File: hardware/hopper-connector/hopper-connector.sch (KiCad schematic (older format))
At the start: 17 parts, among them P1 CONN_01X02, P2 CONN_01X02, P3 CONN_01X05, P4 CONN_01X04, P5 CONN_01X04, Q1 BTS430K2, Q2 BC807-40, U1 LTV-817, U2 LTV-817, U3 LTV-817

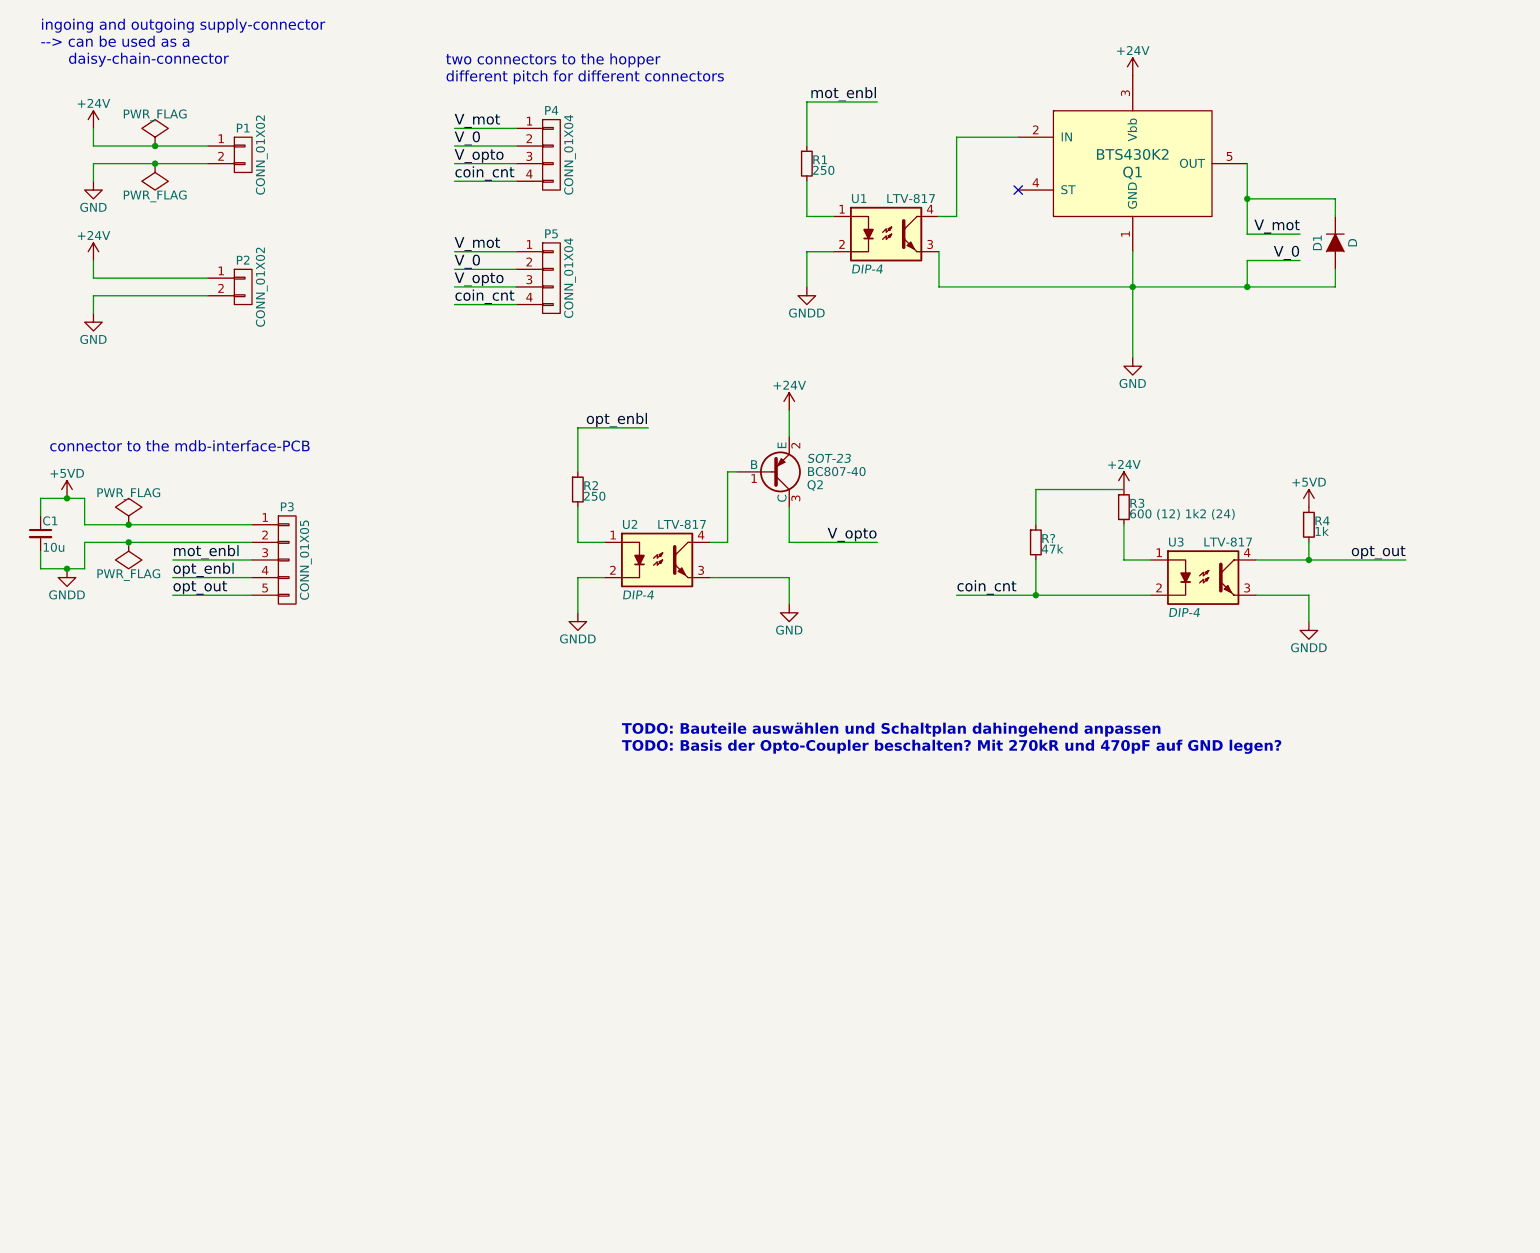
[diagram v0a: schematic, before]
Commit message: circuit now with better couplers and fuse
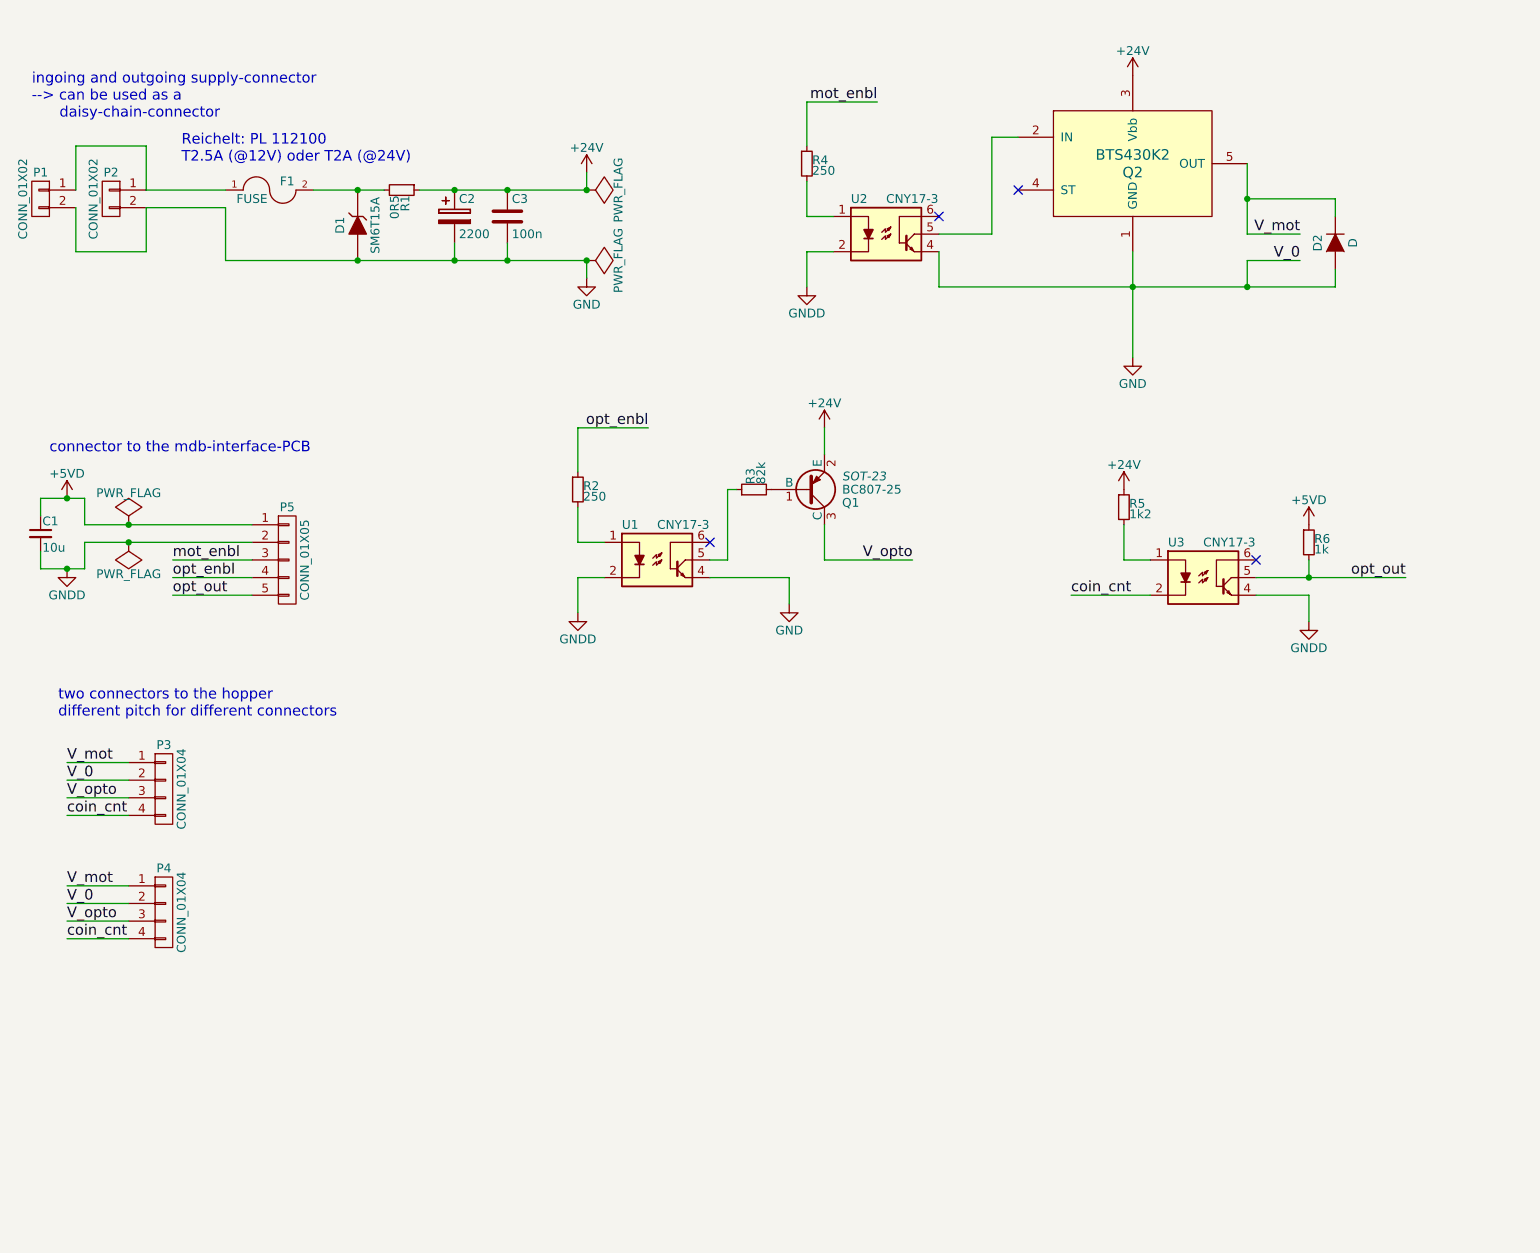
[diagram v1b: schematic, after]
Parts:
- removed R?: 47k, symbol R_Small
- removed U1, U2, U3: LTV-817, DIP-4, symbol LTV-817
- added C2: 2200, symbol CP
- added C3: 100n, symbol C
- added D1: SM6T15A, symbol ZENER
- added F1: FUSE, symbol FUSE
- added R1: 0R5, symbol R_Small
- added R3: 82k, symbol R_Small
- added U1, U2, U3: CNY17-3, symbol CNY17-3
- Q1: renamed from Q2; value BC807-40 -> BC807-25
- R5: renamed from R3; value 600 (12) 1k2 (24) -> 1k2
- renumbered D1 to D2, P2 to P1, P1 to P2, P4 to P3, P5 to P4, P3 to P5, Q1 to Q2, R1 to R4, R4 to R6
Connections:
- net +24V: now also C2.1, C3.1, R1.1; no longer P1.1 (P1), P2.1 (P1)
- net GND: now also C2.2, C3.2, D1.1 (A), U1.4, U2.4
- net GNDD: now also U1.2, U2.2, U3.4
- net coin_cnt: now also U3.2
- net opt_out: now also U3.5
- net at R4.2: now also U2.1
- net at Q2.2 (IN): now also U2.5
- net at R2.2: now also U1.1
- net at Q1.1 (B): now also R3.2
- net at R5.2: now also U3.1
- new net: F1.1, P1.1 (P1), P2.1 (P1)
- new net: R3.1, U1.5
- new net: D1.2 (K), F1.2, R1.2
- no-connect marks 1 -> 4
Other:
- note added: "Reichelt: PL 112100\nT2.5A (@12V) oder T2A (@24V)"
- note removed: "TODO: Bauteile auswählen und Schaltplan dahingehend anpassen\nTODO: Basis der Opto-Coupler beschalten? Mit 270kR und 470pF auf GND legen?"
- moved on the sheet: P1, P2, P3, P4, Q1, R6

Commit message: first real version of schematic
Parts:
- D2: value D -> 1N4004
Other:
- note added: "use stronger TRANSIL?\nThis one will burn before fuse triggers.\n(Only really relevant in case of wrong polarity\nof power supply) Datasheet says the diode\nfails short so at least the protection works..."
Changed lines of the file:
@@
 P 8050 1750
 F 0 "D2" H 8050 1850 50  0000 C CNN
-F 1 "D" H 8050 1650 50  0000 C CNN
+F 1 "1N4004" H 8050 1650 50  0000 C CNN
 F 2 "" H 8050 1750 60  0000 C CNN
 F 3 "" H 8050 1750 60  0000 C CNN
@@
 Connection ~ 3800 1450
 Connection ~ 3800 1850
+Text Notes 2200 2050 0    20   ~ 0
+use stronger TRANSIL?\nThis one will burn before fuse triggers.\n(Only really relevant in case of wrong polarity\nof power supply) Datasheet says the diode\nfails short so at least the protection works...
 $EndSCHEMATC

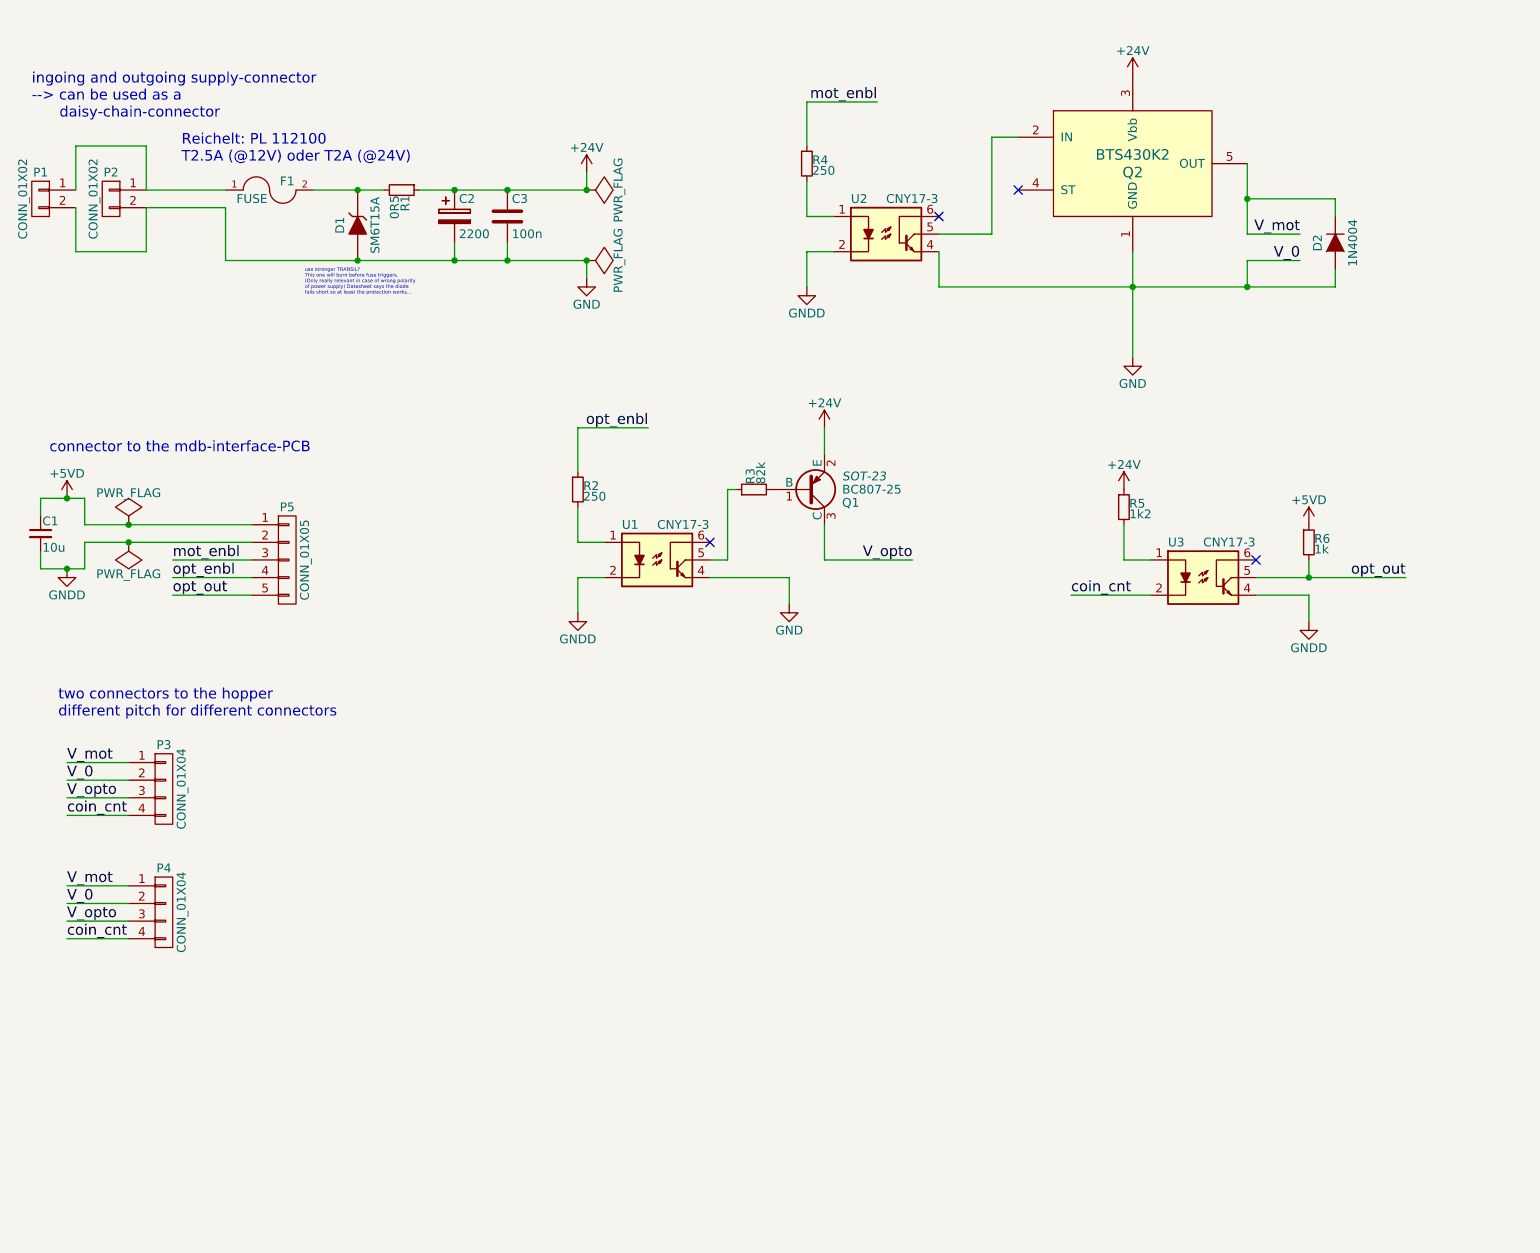
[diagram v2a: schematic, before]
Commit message: added profet status line to connector to mdb-board
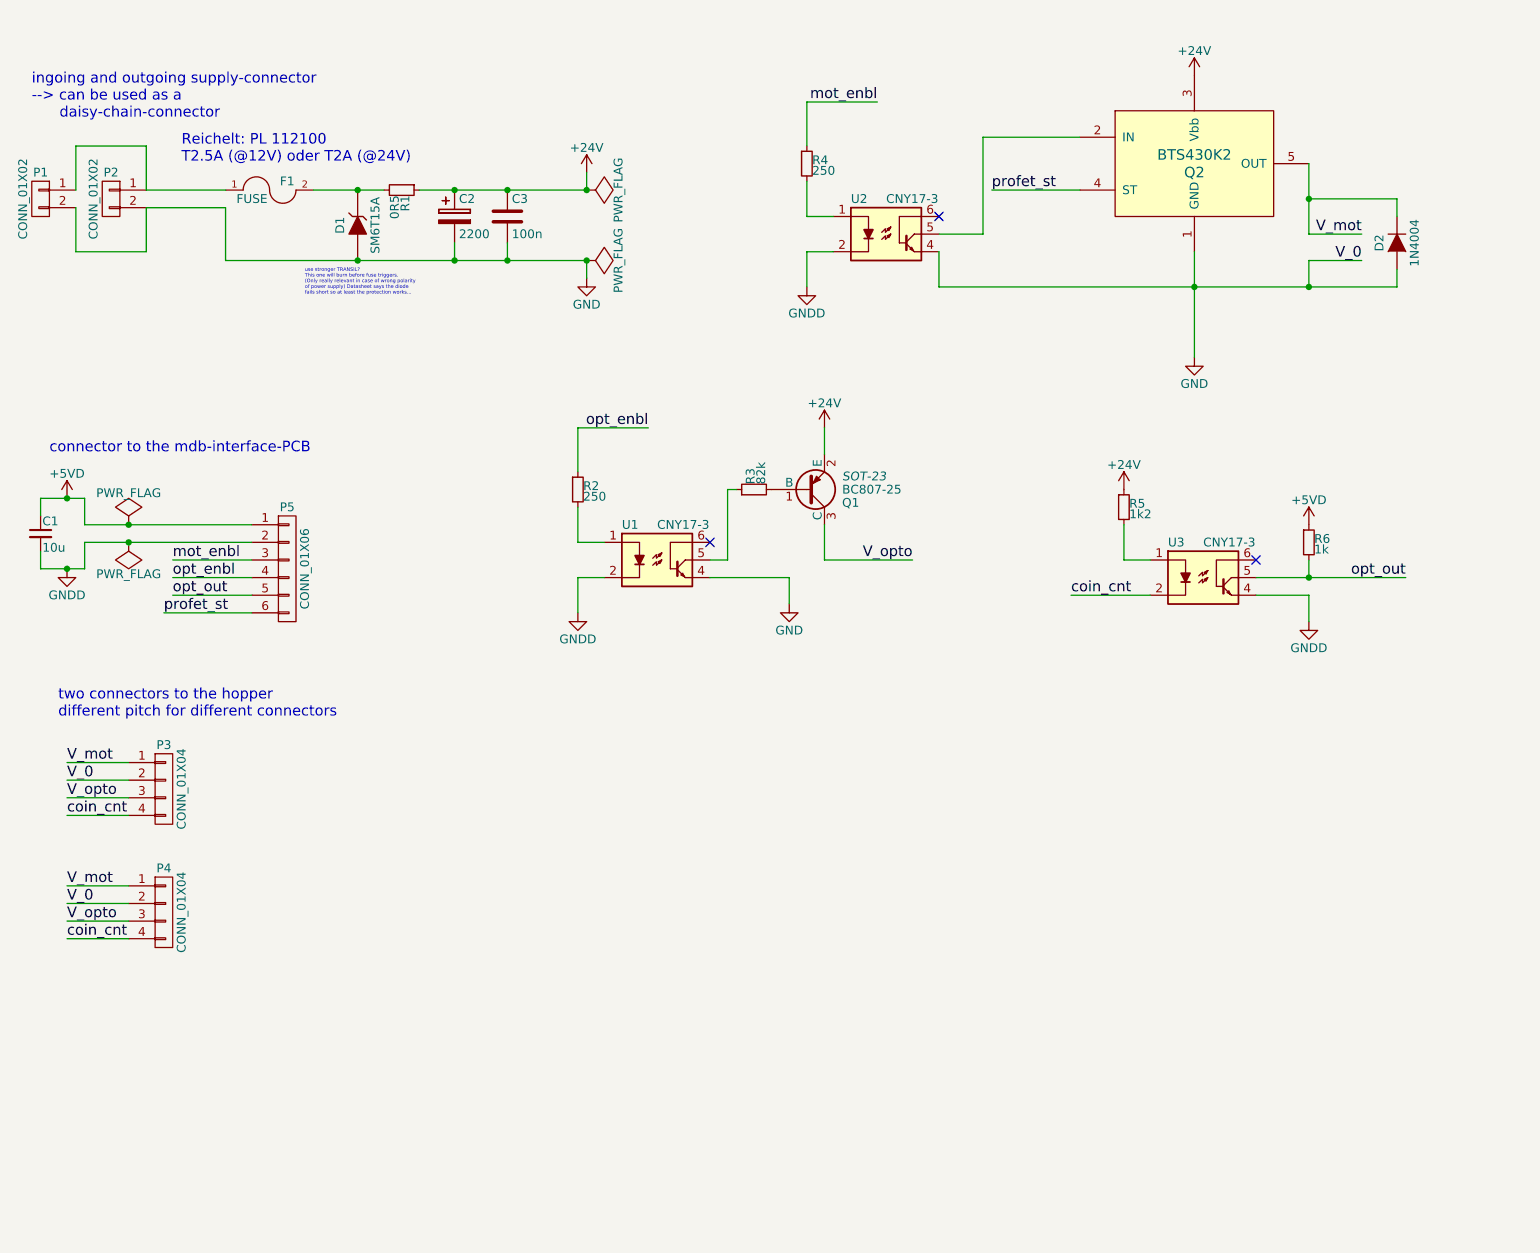
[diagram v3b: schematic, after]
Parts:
- removed P5: CONN_01X05, symbol CONN_01X05
- added P5: CONN_01X06, symbol CONN_01X06
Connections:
- net +5VD: now also P5.1 (P1)
- net GNDD: now also P5.2 (P2)
- net mot_enbl: now also P5.3 (P3)
- net opt_enbl: now also P5.4 (P4)
- net opt_out: now also P5.5 (P5)
- net profet_st: now reaches Q2.4 (ST)
- net profet_st: now also P5.6 (P6)
- no-connect marks 4 -> 3
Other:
- moved on the sheet: D2, Q2
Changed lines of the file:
@@
 Sheet 1 1
 Title "hopper-interface"
-Date "Sa 02 Mai 2015"
-Rev "r0"
+Date "Di 05 Mai 2015"
+Rev "r1"
 Comp "Patrick Kanzler, FAU FabLab"
 Comment1 ""
@@
 L +24V #PWR03
 U 1 1 55462180
-P 6900 800
-F 0 "#PWR03" H 6900 650 50  0001 C CNN
-F 1 "+24V" H 6900 940 50  0000 C CNN
-F 2 "" H 6900 800 60  0000 C CNN
-F 3 "" H 6900 800 60  0000 C CNN
-	1    6900 800
-	1    0    0    -1
-$EndComp
-Text Label 7850 1700 2    60   ~ 0
+P 7250 800
+F 0 "#PWR03" H 7250 650 50  0001 C CNN
+F 1 "+24V" H 7250 940 50  0000 C CNN
+F 2 "" H 7250 800 60  0000 C CNN
+F 3 "" H 7250 800 60  0000 C CNN
+	1    7250 800
+	1    0    0    -1
+$EndComp
+Text Label 8200 1700 2    60   ~ 0
 V_mot
 Wire Wire Line
-	7550 1700 7850 1700
+	7900 1700 8200 1700
 $Comp
 L D D2
 U 1 1 55462252
-P 8050 1750
-F 0 "D2" H 8050 1850 50  0000 C CNN
-F 1 "1N4004" H 8050 1650 50  0000 C CNN
-F 2 "" H 8050 1750 60  0000 C CNN
-F 3 "" H 8050 1750 60  0000 C CNN
-	1    8050 1750
+P 8400 1750
+F 0 "D2" H 8400 1850 50  0000 C CNN
+F 1 "1N4004" H 8400 1650 50  0000 C CNN
+F 2 "" H 8400 1750 60  0000 C CNN
+F 3 "" H 8400 1750 60  0000 C CNN
+	1    8400 1750
 	0    -1   -1   0
 $EndComp
 Wire Wire Line
-	8050 1500 8050 1600
-Wire Wire Line
-	8050 2000 8050 1900
-Text Label 7850 1850 2    60   ~ 0
+	8400 1500 8400 1600
+Wire Wire Line
+	8400 2000 8400 1900
+Text Label 8200 1850 2    60   ~ 0
 V_0
 Wire Wire Line
-	7550 1850 7850 1850
+	7900 1850 8200 1850
 $Comp
 L GND #PWR04
 U 1 1 554623B9
-P 6900 2400
-F 0 "#PWR04" H 6900 2150 50  0001 C CNN
-F 1 "GND" H 6900 2250 50  0000 C CNN
-F 2 "" H 6900 2400 60  0000 C CNN
-F 3 "" H 6900 2400 60  0000 C CNN
-	1    6900 2400
-	1    0    0    -1
-$EndComp
-$Comp
-L CONN_01X05 P5
-U 1 1 5546249B
-P 2100 3550
-F 0 "P5" H 2100 3850 50  0000 C CNN
-F 1 "CONN_01X05" V 2200 3550 50  0000 C CNN
-F 2 "" H 2100 3550 60  0000 C CNN
-F 3 "" H 2100 3550 60  0000 C CNN
-	1    2100 3550
+P 7250 2400
+F 0 "#PWR04" H 7250 2150 50  0001 C CNN
+F 1 "GND" H 7250 2250 50  0000 C CNN
+F 2 "" H 7250 2400 60  0000 C CNN
+F 3 "" H 7250 2400 60  0000 C CNN
+	1    7250 2400
 	1    0    0    -1
 $EndComp
@@
 V_opto
 Wire Wire Line
-	8050 1500 7550 1500
-Wire Wire Line
-	7550 1850 7550 2000
+	8400 1500 7900 1500
+Wire Wire Line
+	7900 1850 7900 2000
 Wire Wire Line
 	5800 1800 5800 2000
@@
 	5150 2800 5150 2950
 Wire Wire Line
-	5800 2000 8050 2000
-NoConn ~ 6250 1450
-Connection ~ 7550 1500
-Connection ~ 7550 2000
-Connection ~ 6900 2000
+	5800 2000 8400 2000
+Connection ~ 7900 1500
+Connection ~ 7900 2000
+Connection ~ 7250 2000
 $Comp
 L PROFET Q2
 U 1 1 5546C062
-P 6900 1300
-F 0 "Q2" H 6900 1250 60  0000 C CNN
-F 1 "BTS430K2" H 6900 1350 60  0000 C CNN
-F 2 "" H 6900 1300 60  0000 C CNN
-F 3 "" H 6900 1300 60  0000 C CNN
-	1    6900 1300
+P 7250 1300
+F 0 "Q2" H 7250 1250 60  0000 C CNN
+F 1 "BTS430K2" H 7250 1350 60  0000 C CNN
+F 2 "" H 7250 1300 60  0000 C CNN
+F 3 "" H 7250 1300 60  0000 C CNN
+	1    7250 1300
 	1    0    0    -1
 $EndComp
@@
 $EndComp
 Wire Wire Line
-	6250 1150 6100 1150
-Wire Wire Line
-	6100 1150 6100 1700
-Wire Wire Line
-	6100 1700 5800 1700
-Wire Wire Line
-	7550 1300 7550 1700
-Wire Wire Line
-	6900 1800 6900 2400
+	7900 1300 7900 1700
+Wire Wire Line
+	7250 1800 7250 2400
 NoConn ~ 4500 3450
 NoConn ~ 5800 1600
@@
 Text Notes 2200 2050 0    20   ~ 0
 use stronger TRANSIL?\nThis one will burn before fuse triggers.\n(Only really relevant in case of wrong polarity\nof power supply) Datasheet says the diode\nfails short so at least the protection works...
+Text Label 6100 1450 0    60   ~ 0
+profet_st
+Wire Wire Line
+	6600 1450 6100 1450
+Wire Wire Line
+	6600 1150 6050 1150
+Wire Wire Line
+	6050 1150 6050 1700
+Wire Wire Line
+	6050 1700 5800 1700
+$Comp
+L CONN_01X06 P5
+U 1 1 55487484
+P 2100 3600
+F 0 "P5" H 2100 3950 50  0000 C CNN
+F 1 "CONN_01X06" V 2200 3600 50  0000 C CNN
+F 2 "" H 2100 3600 60  0000 C CNN
+F 3 "" H 2100 3600 60  0000 C CNN
+	1    2100 3600
+	1    0    0    -1
+$EndComp
+Text Label 1400 3850 0    60   ~ 0
+profet_st
+Wire Wire Line
+	1900 3850 1400 3850
 $EndSCHEMATC
